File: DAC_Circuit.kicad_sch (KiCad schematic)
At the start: 40 parts, among them IC4 DAC5652IPFB, J6 Conn_01x03_Pin, J7 Conn_01x03_Pin, J8 SMA Connector, J9 SMA Connector, U4 LMH6702MA, U5 LMH6702MA

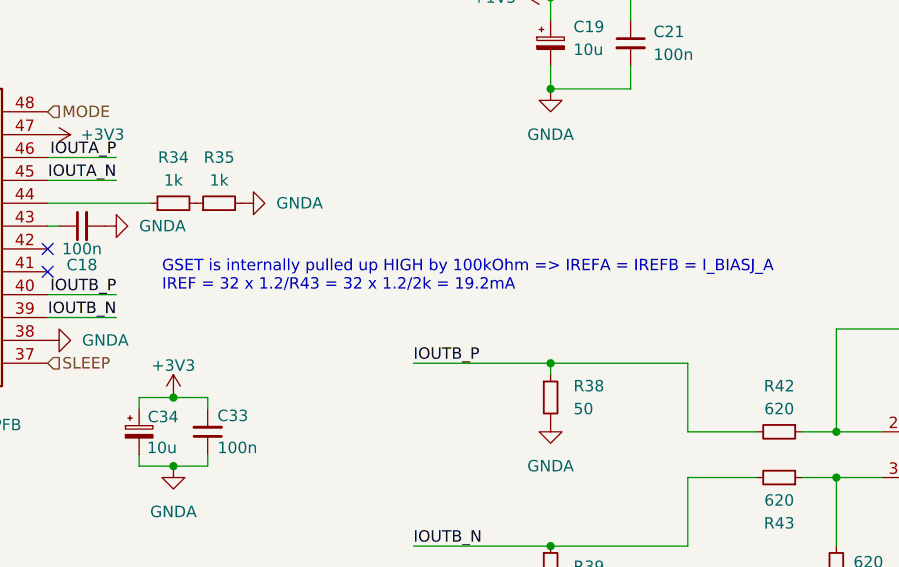
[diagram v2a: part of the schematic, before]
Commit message: Review photos and Mezzaninne spelling mistake fixed
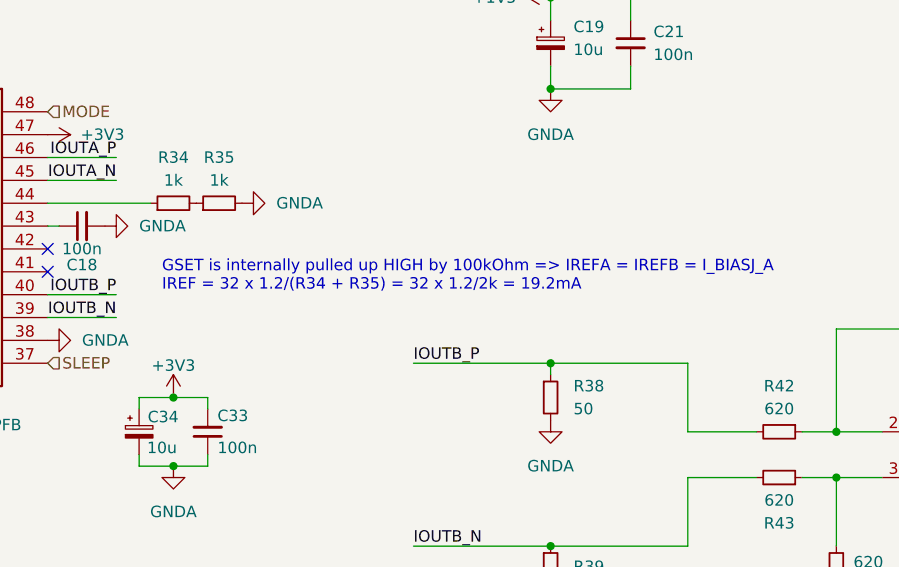
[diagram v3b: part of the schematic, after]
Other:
- note added: "GSET is internally pulled up HIGH by 100kOhm => IREFA = IREFB = I_BIASJ_A IREF = 32 x 1.2/(R34 + R35) = 32 x 1.2/2k = 19.2mA"
- note removed: "GSET is internally pulled up HIGH by 100kOhm => IREFA = IREFB = I_BIASJ_A IREF = 32 x 1.2/R43 = 32 x 1.2/2k = 19.2mA"
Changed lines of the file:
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@@
 		)
 	)
-	(text "GSET is internally pulled up HIGH by 100kOhm => IREFA = IREFB = I_BIASJ_A\nIREF = 32 x 1.2/R43 = 32 x 1.2/2k = 19.2mA"
+	(text "GSET is internally pulled up HIGH by 100kOhm => IREFA = IREFB = I_BIASJ_A\nIREF = 32 x 1.2/(R34 + R35) = 32 x 1.2/2k = 19.2mA"
 		(exclude_from_sim no)
 		(at 132.08 99.568 0)

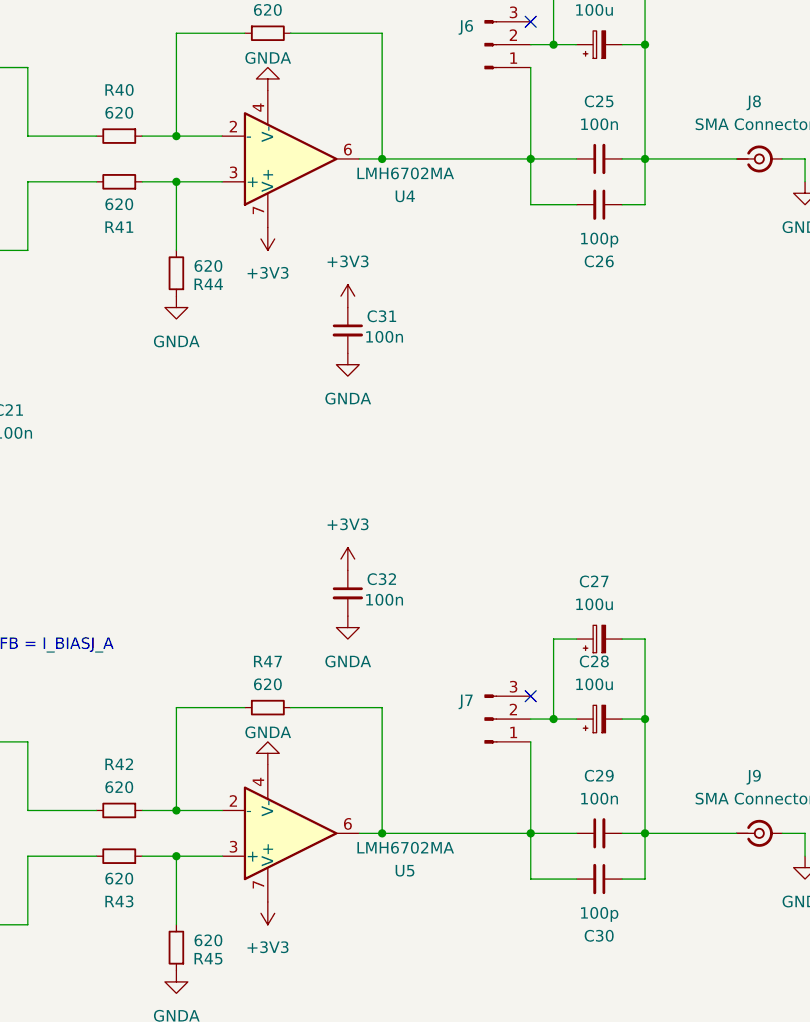
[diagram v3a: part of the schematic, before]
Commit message: Error in schematic, DAC output opamp is LMH6720, not LMH6702
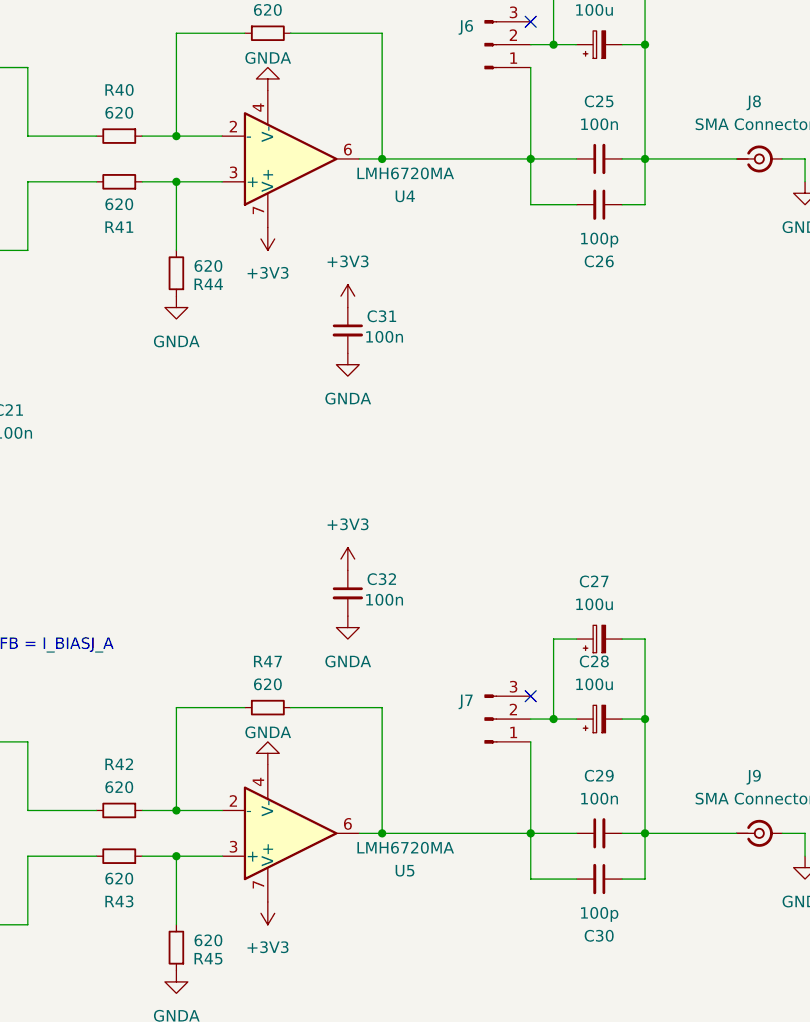
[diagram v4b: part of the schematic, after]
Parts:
- U4, U5: value LMH6702MA -> LMH6720MA
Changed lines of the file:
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@@
 			)
 		)
-		(property "Value" "LMH6702MA"
+		(property "Value" "LMH6720MA"
 			(at 232.41 121.031 0)
 			(effects
@@
 			)
 		)
-		(property "Value" "LMH6702MA"
+		(property "Value" "LMH6720MA"
 			(at 232.41 46.101 0)
 			(effects

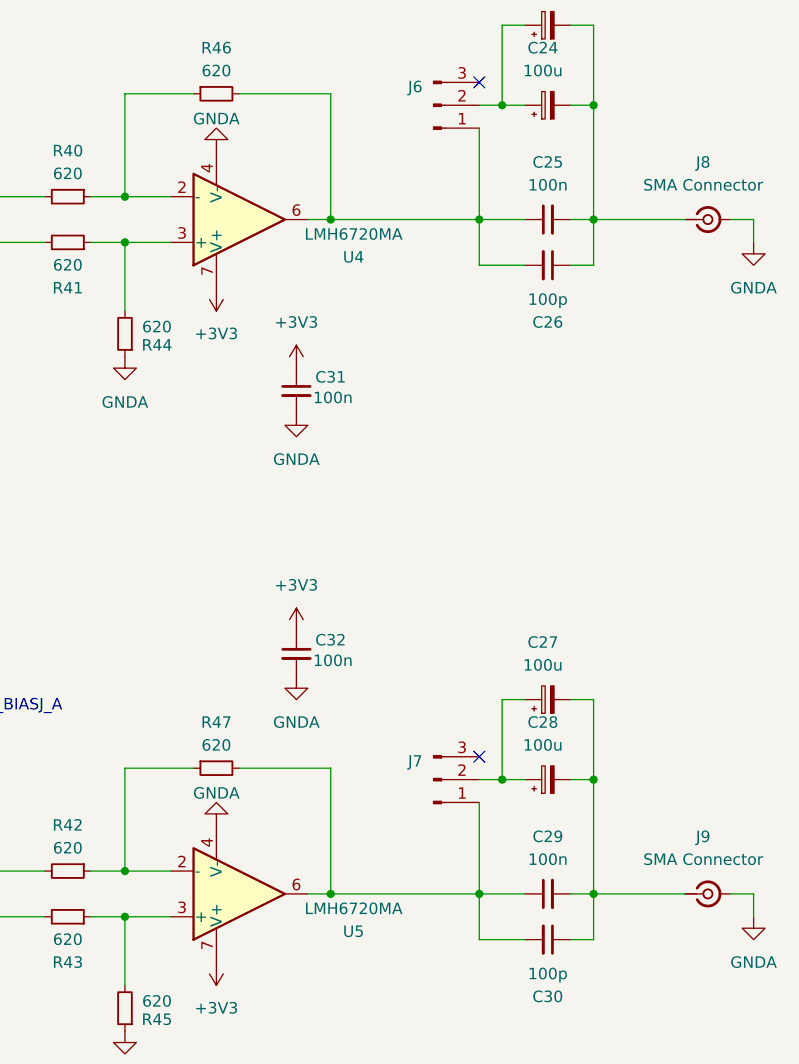
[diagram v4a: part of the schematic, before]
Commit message: Rev 1.1
Multiple changes are made, as per suggestions made by the redditors of r/PrintedCircuitBoards. Firstly, two 50 ohm resistors were added in series with the DAC output in order to comply with the minimum peak output current of the op-amps of 50mA. Secondly, two M3 mounting holes were added in order to have the possibility to add standoffs. Thirdly, a clearance issue regarding jumpers near the LPC connector on the ML602 board was fixed by changing the board geometry to include a cutout for these.

Some other things to look into are the use of some ferrite beads for supplies of the analog ICs.
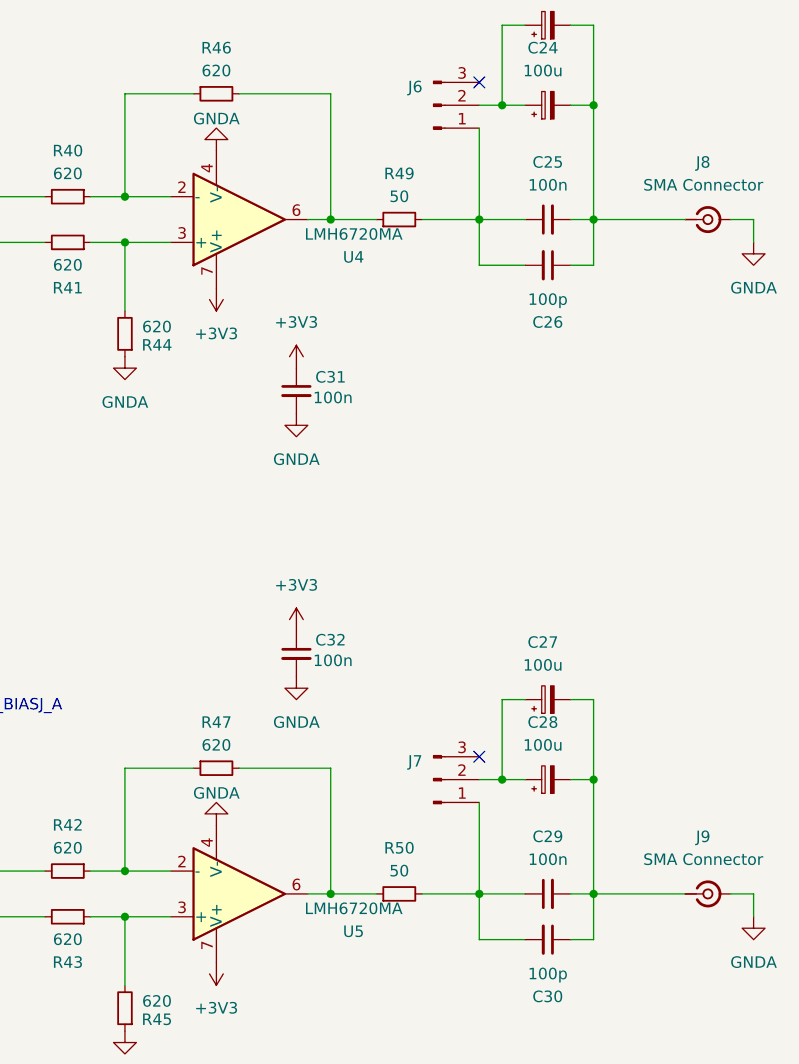
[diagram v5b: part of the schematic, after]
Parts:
- added R49, R50: 50, Resistor_SMD:R_0805_2012Metric_Pad1.20x1.40mm_HandSolder, symbol Device:R_Small
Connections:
- net at C29.1, C30.2, J7.1 (Pin_1): now also R50.2; no longer R47.2, U5.6
- net at C25.1, C26.2, J6.1 (Pin_1): now also R49.2; no longer R46.2, U4.6
- new net: R46.2, R49.1, U4.6
- new net: R47.2, R50.1, U5.6
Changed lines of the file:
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@@
 	)
 	(junction
-		(at 229.87 119.38)
+		(at 175.26 153.67)
 		(diameter 0)
 		(color 0 0 0 0)
 	)
 	(junction
-		(at 175.26 153.67)
+		(at 259.08 119.38)
 		(diameter 0)
 		(color 0 0 0 0)
 	)
 	(junction
-		(at 259.08 119.38)
+		(at 248.92 31.75)
 		(diameter 0)
 		(color 0 0 0 0)
 	)
 	(junction
-		(at 248.92 31.75)
+		(at 229.87 44.45)
 		(diameter 0)
 		(color 0 0 0 0)
@@
 	)
 	(junction
-		(at 207.01 121.92)
+		(at 229.87 119.38)
 		(diameter 0)
 		(color 0 0 0 0)
 	)
 	(junction
-		(at 175.26 143.51)
+		(at 207.01 121.92)
 		(diameter 0)
 		(color 0 0 0 0)
 	)
 	(junction
-		(at 229.87 44.45)
+		(at 175.26 143.51)
 		(diameter 0)
 		(color 0 0 0 0)
@@
 	(wire
 		(pts
+			(xy 240.03 119.38) (xy 246.38 119.38)
+		)
+		(stroke
+			(width 0)
+			(type default)
+		)
+	)
+	(wire
+		(pts
 			(xy 207.01 46.99) (xy 207.01 54.61)
 		)
@@
 	(wire
 		(pts
-			(xy 229.87 119.38) (xy 246.38 119.38)
-		)
-		(stroke
-			(width 0)
-			(type default)
-		)
-	)
-	(wire
-		(pts
 			(xy 256.54 44.45) (xy 259.08 44.45)
 		)
@@
 	(wire
 		(pts
+			(xy 229.87 44.45) (xy 234.95 44.45)
+		)
+		(stroke
+			(width 0)
+			(type default)
+		)
+	)
+	(wire
+		(pts
 			(xy 31.75 123.19) (xy 31.75 124.46)
 		)
@@
 	(wire
 		(pts
+			(xy 240.03 44.45) (xy 246.38 44.45)
+		)
+		(stroke
+			(width 0)
+			(type default)
+		)
+	)
+	(wire
+		(pts
+			(xy 229.87 119.38) (xy 234.95 119.38)
+		)
+		(stroke
+			(width 0)
+			(type default)
+		)
+	)
+	(wire
+		(pts
 			(xy 175.26 54.61) (xy 190.5 54.61)
 		)
@@
 	(wire
 		(pts
-			(xy 229.87 44.45) (xy 246.38 44.45)
-		)
-		(stroke
-			(width 0)
-			(type default)
-		)
-	)
-	(wire
-		(pts
 			(xy 259.08 44.45) (xy 269.24 44.45)
 		)
@@
 	)
 	(symbol
+		(lib_id "Device:R_Small")
+		(at 237.49 44.45 90)
+		(unit 1)
+		(exclude_from_sim no)
+		(in_bom yes)
+		(on_board yes)
+		(dnp no)
+		(fields_autoplaced yes)
+		(property "Reference" "R49"
+			(at 237.49 39.37 90)
+			(effects
+				(font
+					(size 1.27 1.27)
+				)
+			)
+		)
+		(property "Value" "50"
+			(at 237.49 41.91 90)
+			(effects
+				(font
+					(size 1.27 1.27)
+				)
+			)
+		)
+		(property "Footprint" "Resistor_SMD:R_0805_2012Metric_Pad1.20x1.40mm_HandSolder"
+			(at 237.49 44.45 0)
+			(effects
+				(font
+					(size 1.27 1.27)
+				)
+				(hide yes)
+			)
+		)
+		(property "Datasheet" "~"
+			(at 237.49 44.45 0)
+			(effects
+				(font
+					(size 1.27 1.27)
+				)
+				(hide yes)
+			)
+		)
+		(property "Description" "Resistor, small symbol"
+			(at 237.49 44.45 0)
+			(effects
+				(font
+					(size 1.27 1.27)
+				)
+				(hide yes)
+			)
+		)
+		(property "Mouser Link" "https://ro.mouser.com/ProductDetail/Vishay-Dale/CRCW080550R0FKTA?qs=sGAEpiMZZMtlubZbdhIBIHdFOaufIt3b7Pt0cew8QLQ%3D"
+			(at 237.49 44.45 0)
+			(effects
+				(font
+					(size 1.27 1.27)
+				)
+				(hide yes)
+			)
+		)
+		(pin "1"
+		)
+		(pin "2"
+		)
+		(instances
+			(project "ML605_LPC_Board_wADC_DAC"
+				(path "/35bdcd8d-8b21-4a24-9357-7d92e5ad0993/83873eff-166e-4e25-b51a-e3caec22538a"
+					(reference "R49")
+					(unit 1)
+				)
+			)
+		)
+	)
+	(symbol
 		(lib_id "Device:C_Small")
 		(at 254 49.53 270)
@@
 					(unit 1)
 				)
+			)
+		)
+	)
+	(symbol
+		(lib_id "Device:R_Small")
+		(at 237.49 119.38 90)
+		(unit 1)
+		(exclude_from_sim no)
+		(in_bom yes)
+		(on_board yes)
+		(dnp no)
+		(fields_autoplaced yes)
+		(property "Reference" "R50"
+			(at 237.49 114.3 90)
+			(effects
+				(font
+					(size 1.27 1.27)
+				)
+			)
+		)
+		(property "Value" "50"
+			(at 237.49 116.84 90)
+			(effects
+				(font
+					(size 1.27 1.27)
+				)
+			)
+		)
+		(property "Footprint" "Resistor_SMD:R_0805_2012Metric_Pad1.20x1.40mm_HandSolder"
+			(at 237.49 119.38 0)
+			(effects
+				(font
+					(size 1.27 1.27)
+				)
+				(hide yes)
+			)
+		)
+		(property "Datasheet" "~"
+			(at 237.49 119.38 0)
+			(effects
+				(font
+					(size 1.27 1.27)
+				)
+				(hide yes)
+			)
+		)
+		(property "Description" "Resistor, small symbol"
+			(at 237.49 119.38 0)
+			(effects
+				(font
+					(size 1.27 1.27)
+				)
+				(hide yes)
+			)
+		)
+		(property "Mouser Link" "https://ro.mouser.com/ProductDetail/Vishay-Dale/CRCW080550R0FKTA?qs=sGAEpiMZZMtlubZbdhIBIHdFOaufIt3b7Pt0cew8QLQ%3D"
+			(at 237.49 119.38 0)
+			(effects
+				(font
+					(size 1.27 1.27)
+				)
+				(hide yes)
+			)
+		)
+		(pin "1"
+		)
+		(pin "2"
+		)
+		(instances
+			(project "ML605_LPC_Board_wADC_DAC"
+				(path "/35bdcd8d-8b21-4a24-9357-7d92e5ad0993/83873eff-166e-4e25-b51a-e3caec22538a"
+					(reference "R50")
+					(unit 1)
+				)
